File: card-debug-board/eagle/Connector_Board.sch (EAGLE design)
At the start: 41 parts, among them J1 ORESAT-DEBUG-CONNECTOR-MIRROR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, J3 USB_A_SMT_FEMALE, Q1 MOSFET-PCH-SOT23-6, SW1 B3F-1000, U1 FT230XS-R

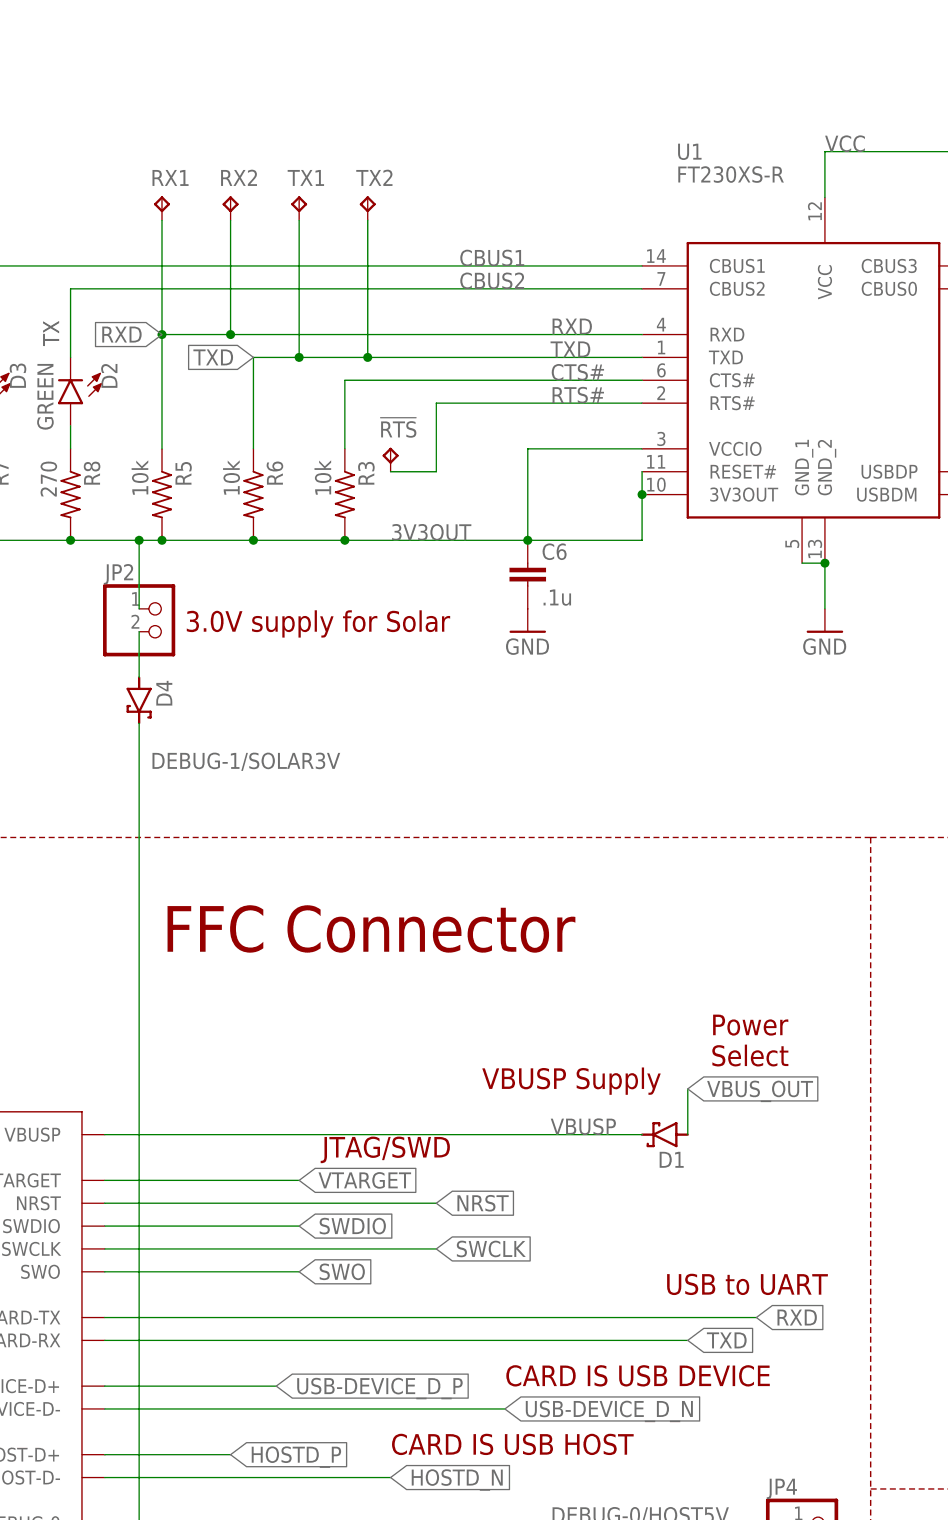
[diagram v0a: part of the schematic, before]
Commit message: Added 10k resistor to the FTDI's TXD line so that we don't accidentally power the card through the transmit line)
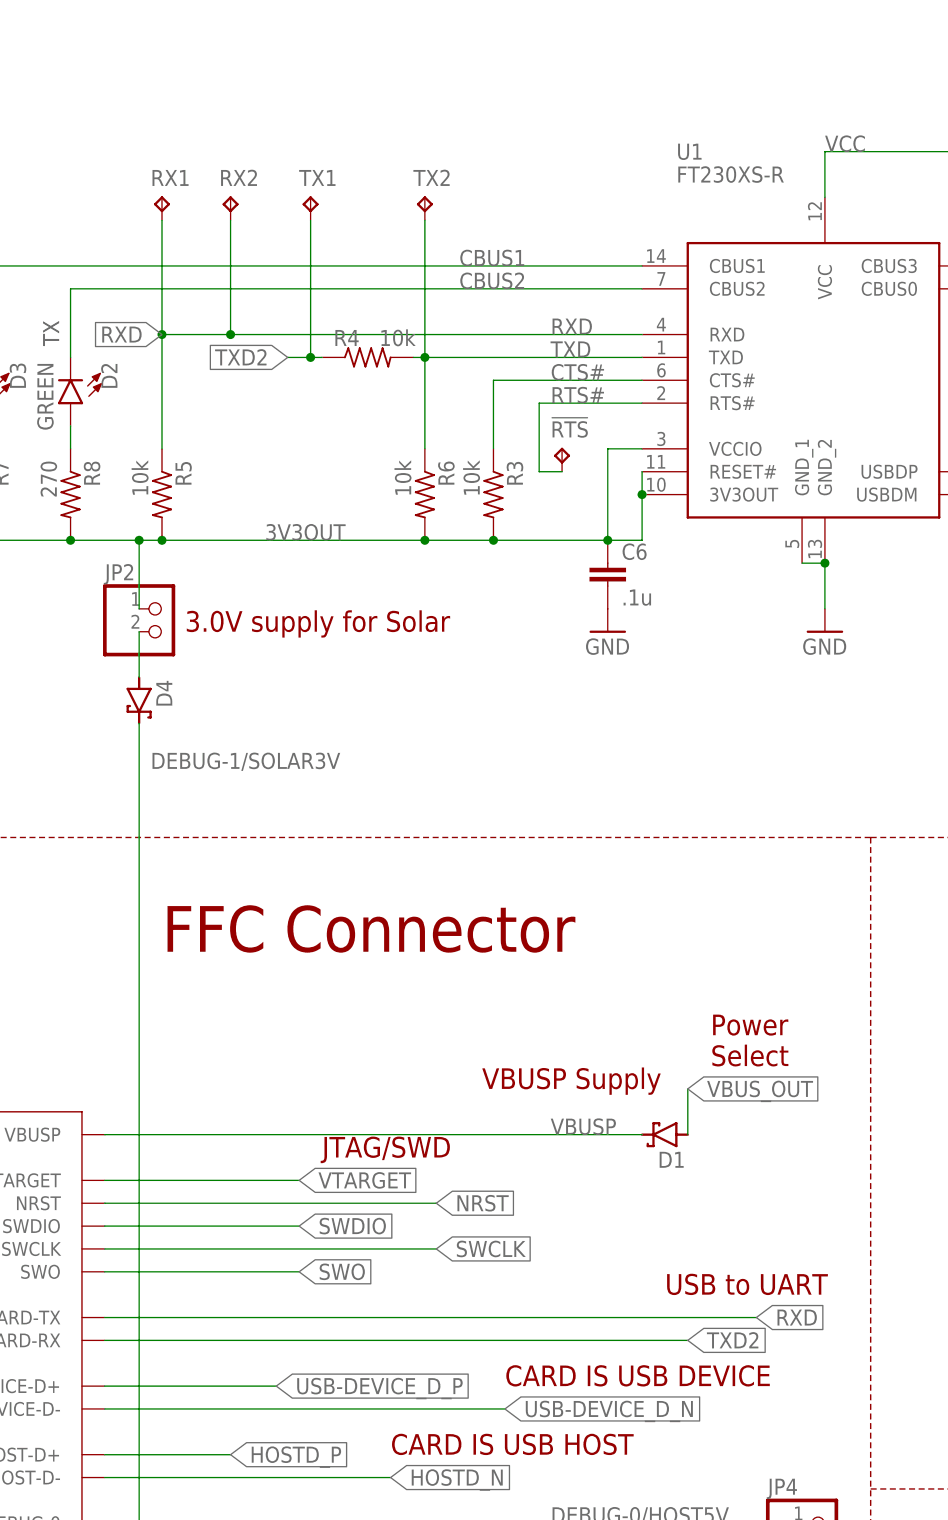
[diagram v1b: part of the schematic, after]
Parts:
- added R4: 10k, oresat-rcl:R-US_0603-C-NOSILK
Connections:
- new net TXD2: J1.CARD-RX, R4.1, TX1.TP
- net TXD: now also R4.2; no longer J1.CARD-RX, TX1.TP
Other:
- moved on the sheet: C6, R3, R6, TX1, TX2, ~{RTS}

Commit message: Fixed RX/TX screw up (updated debug connector).
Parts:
- J1: value ORESAT-DEBUG-CONNECTOR-MIRRORED-SOLAR -> ORESAT-DEBUG-CONNECTOR-MIRRORED-ALL; device oresat-debug-connector:ORESAT-DEBUG-CONNECTOR-MIRRORED-SOLAR -> oresat-debug-connector:ORESAT-DEBUG-CONNECTOR-MIRRORED-ALL
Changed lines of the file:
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@@
 <setting verticaltext="up"/>
 </settings>
-<grid distance="0.05" unitdist="inch" unit="inch" style="lines" multiple="2" display="no" altdistance="0.01" altunitdist="inch" altunit="inch"/>
+<grid distance="0.1" unitdist="inch" unit="inch" style="lines" multiple="1" display="no" altdistance="0.01" altunitdist="inch" altunit="inch"/>
 <layers>
 <layer number="1" name="Top" color="4" fill="1" visible="no" active="no"/>
@@
 <part name="GND8" library="supply1" library_urn="urn:adsk.eagle:library:371" deviceset="GND" device=""/>
 <part name="GND9" library="supply1" library_urn="urn:adsk.eagle:library:371" deviceset="GND" device=""/>
-<part name="J1" library="oresat-debug-connector" deviceset="ORESAT-DEBUG-CONNECTOR-MIRRORED" device="-SOLAR" value="ORESAT-DEBUG-CONNECTOR-MIRRORED-SOLAR">
+<part name="J1" library="oresat-debug-connector" deviceset="ORESAT-DEBUG-CONNECTOR-MIRRORED" device="-ALL" value="ORESAT-DEBUG-CONNECTOR-MIRRORED-ALL">
 <attribute name="DESCRIPTION" value="20 Position FPC Connector Contacts, Bottom 0.020&quot; (0.50mm) Surface Mount, Right Angle"/>
 <attribute name="DIGI-KEY_PART_NUMBER" value="A100287CT-ND"/>
